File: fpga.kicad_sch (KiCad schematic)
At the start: 8 parts

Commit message: Added FPGA power component
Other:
- title: (none) -> Field-programmable gate array
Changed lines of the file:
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@@
 (kicad_sch (version 20230121) (generator eeschema)
   (paper "A3")
+  (title_block
+    (title "Field-programmable gate array")
+  )
   (wire (pts (xy 74.93 177.8) (xy 85.09 177.8))
     (stroke (width 0) (type default))

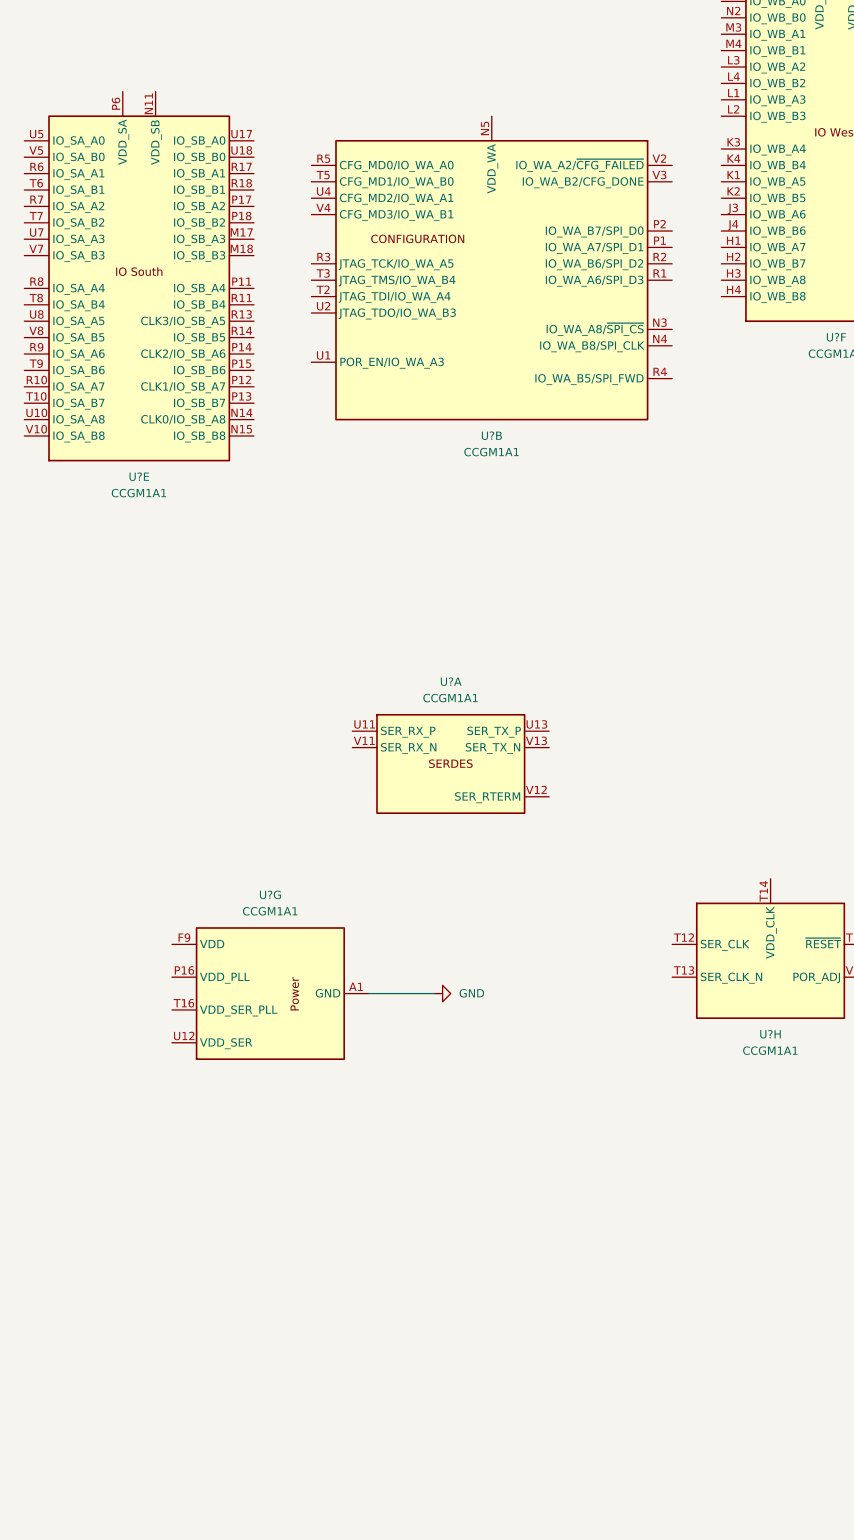
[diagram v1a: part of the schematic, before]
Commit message: Moved USB-C connector to root sheet
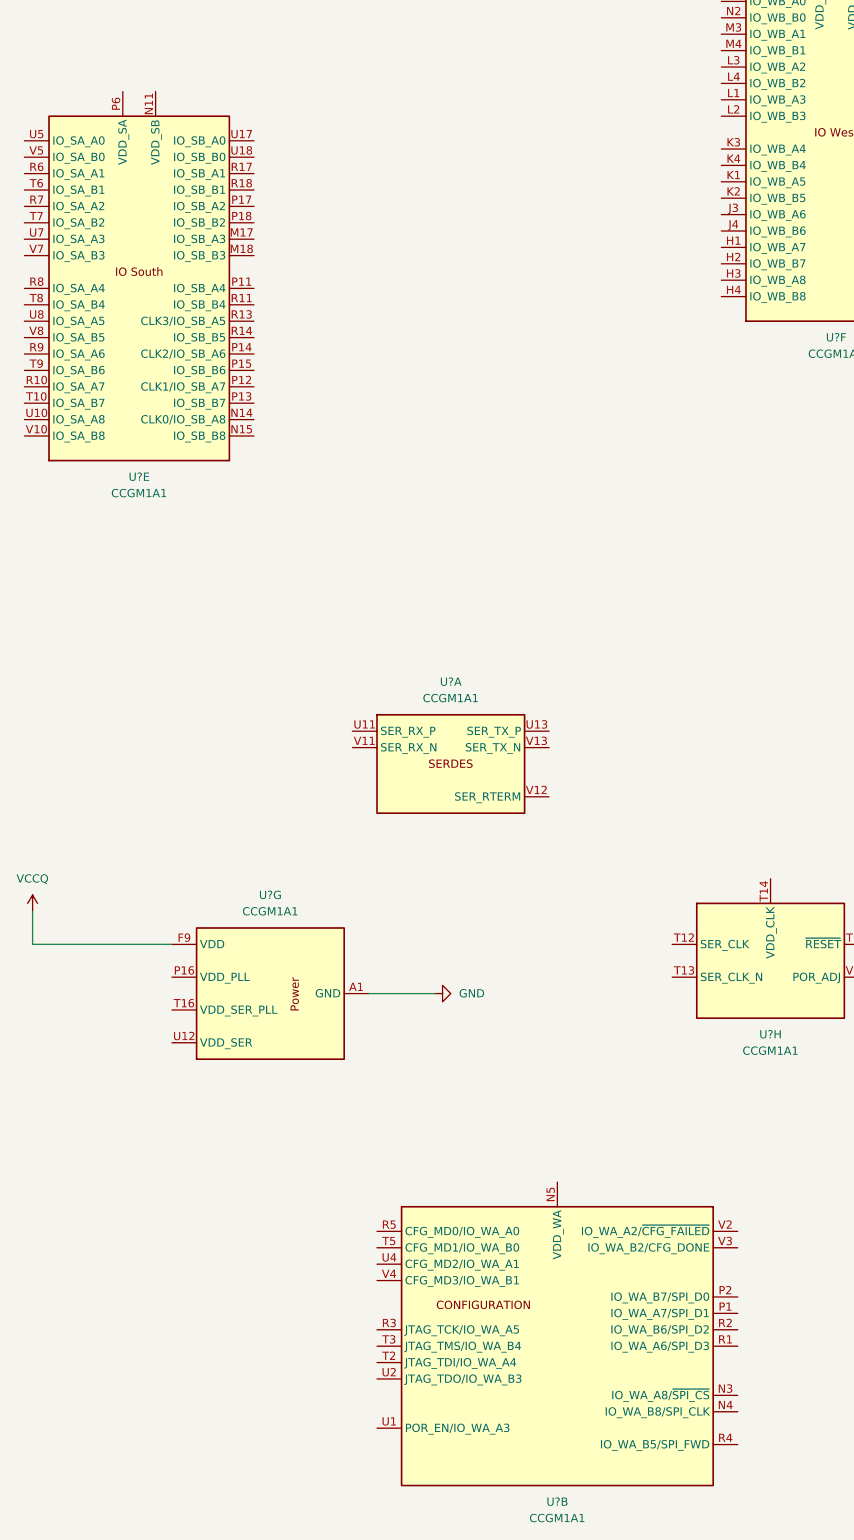
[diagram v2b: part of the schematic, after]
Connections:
- net VCCQ: now reaches U?.F9 (VDD), U?.G10 (VDD), U?.G12 (VDD), U?.G6 (VDD), U?.G8 (VDD), U?.H11 (VDD), U?.H13 (VDD), U?.H7 (VDD), U?.H9 (VDD), U?.J10 (VDD), U?.J12 (VDD), U?.J6 (VDD), U?.J8 (VDD), U?.K11 (VDD), U?.K13 (VDD), U?.K7 (VDD), U?.K9 (VDD), U?.L10 (VDD), U?.L12 (VDD), U?.L6 (VDD), U?.L8 (VDD), U?.M11 (VDD), U?.M13 (VDD), U?.M7 (VDD), U?.M9 (VDD), U?.N10 (VDD), U?.N6 (VDD), U?.N8 (VDD)
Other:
- moved on the sheet: U?B
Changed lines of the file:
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@@
+    (stroke (width 0) (type default))
+  )
+  (wire (pts (xy 22.86 170.18) (xy 44.45 170.18))
+    (stroke (width 0) (type default))
+  )
+  (wire (pts (xy 22.86 165.1) (xy 22.86 170.18))
     (stroke (width 0) (type default))
   )
@@
     )
   )
-  (symbol (lib_id "FPGA_CologneChip_GateMate:CCGM1A1") (at 93.98 67.31 0) (unit 2)
+  (symbol (lib_id "FPGA_CologneChip_GateMate:CCGM1A1") (at 104.14 232.41 0) (unit 2)
     (in_bom yes) (on_board yes) (dnp no) (fields_autoplaced)
-    (property "Reference" "U?" (at 93.98 91.44 0)
+    (property "Reference" "U?" (at 104.14 256.54 0)
       (effects (font (size 1.27 1.27)))
     )
-    (property "Value" "CCGM1A1" (at 93.98 93.98 0)
+    (property "Value" "CCGM1A1" (at 104.14 259.08 0)
       (effects (font (size 1.27 1.27)))
     )
-    (property "Footprint" "Package_BGA:BGA-324_15.0x15.0mm_Layout18x18_P0.8mm_Ball0.45mm_Pad0.4mm_NSMD" (at 88.9 50.8 0)
+    (property "Footprint" "Package_BGA:BGA-324_15.0x15.0mm_Layout18x18_P0.8mm_Ball0.45mm_Pad0.4mm_NSMD" (at 99.06 215.9 0)
       (effects (font (size 1.27 1.27)) hide)
     )
-    (property "Datasheet" "https://colognechip.com/docs/ds1001-gatemate1-datasheet-2022-05.pdf" (at 93.98 59.69 0)
+    (property "Datasheet" "https://colognechip.com/docs/ds1001-gatemate1-datasheet-2022-05.pdf" (at 104.14 224.79 0)
       (effects (font (size 1.27 1.27)) hide)
     )
@@
         )
       )
+    )
+  )
+  (symbol (lib_id "power:VCCQ") (at 22.86 165.1 0) (unit 1)
+    (in_bom yes) (on_board yes) (dnp no) (fields_autoplaced)
+    (property "Reference" "#PWR040" (at 22.86 168.91 0)
+      (effects (font (size 1.27 1.27)) hide)
+    )
+    (property "Value" "VCCQ" (at 22.86 160.02 0)
+      (effects (font (size 1.27 1.27)))
+    )
+    (property "Footprint" "" (at 22.86 165.1 0)
+      (effects (font (size 1.27 1.27)) hide)
+    )
+    (property "Datasheet" "" (at 22.86 165.1 0)
+      (effects (font (size 1.27 1.27)) hide)
+    )
+    (pin "1")
+    (instances
+      (project "drone"
+        (path "/d34d8324-c983-4098-8d7e-5c2fbd34794d/41f449fb-b4c2-4d53-966f-b49577e16db6"
+          (reference "#PWR040") (unit 1)
+        )
+      )

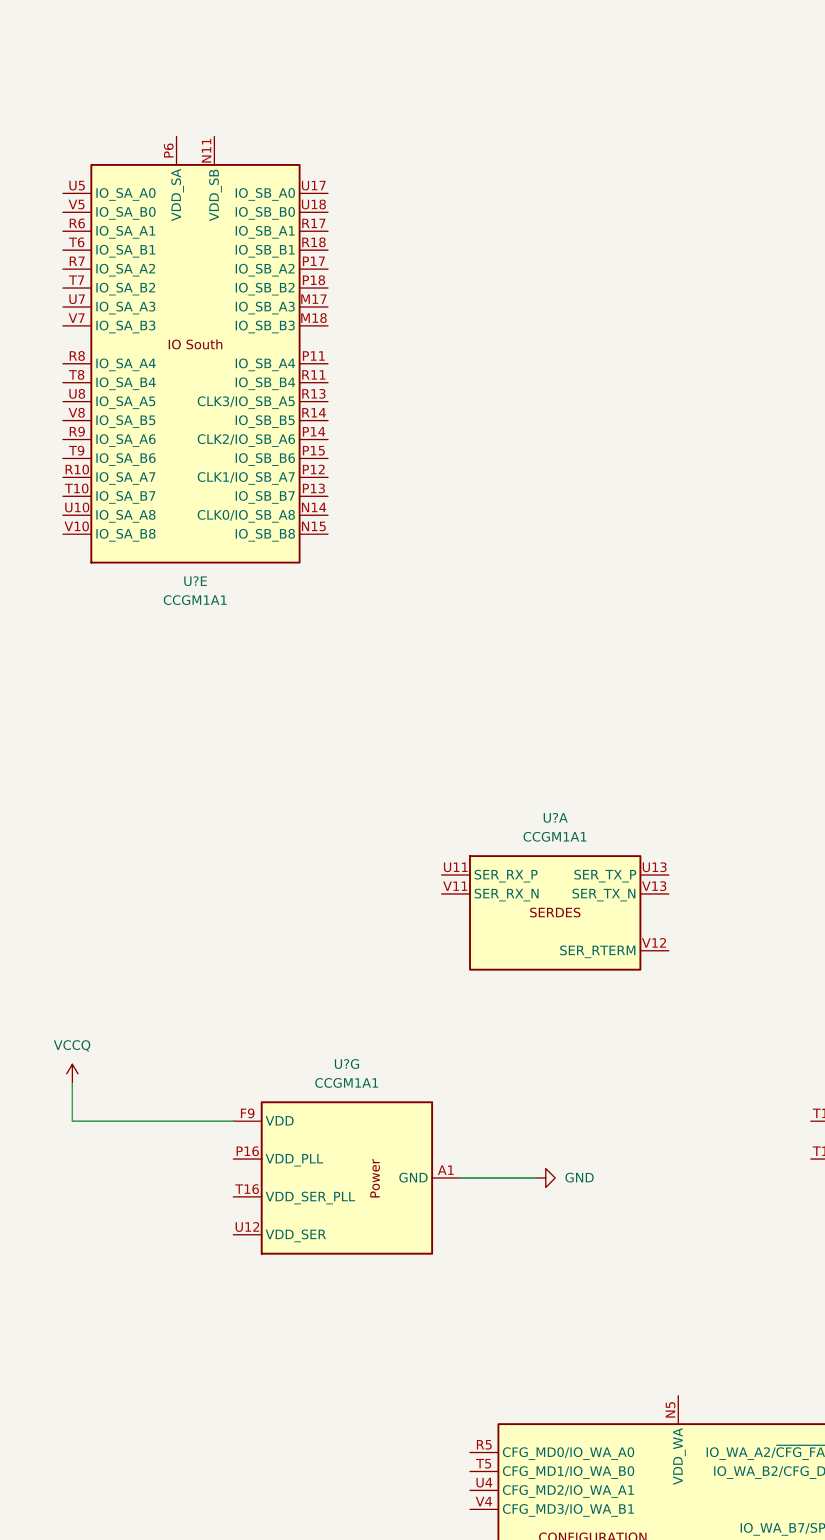
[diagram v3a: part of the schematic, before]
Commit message: Replacing global power labels with hierarchical pins
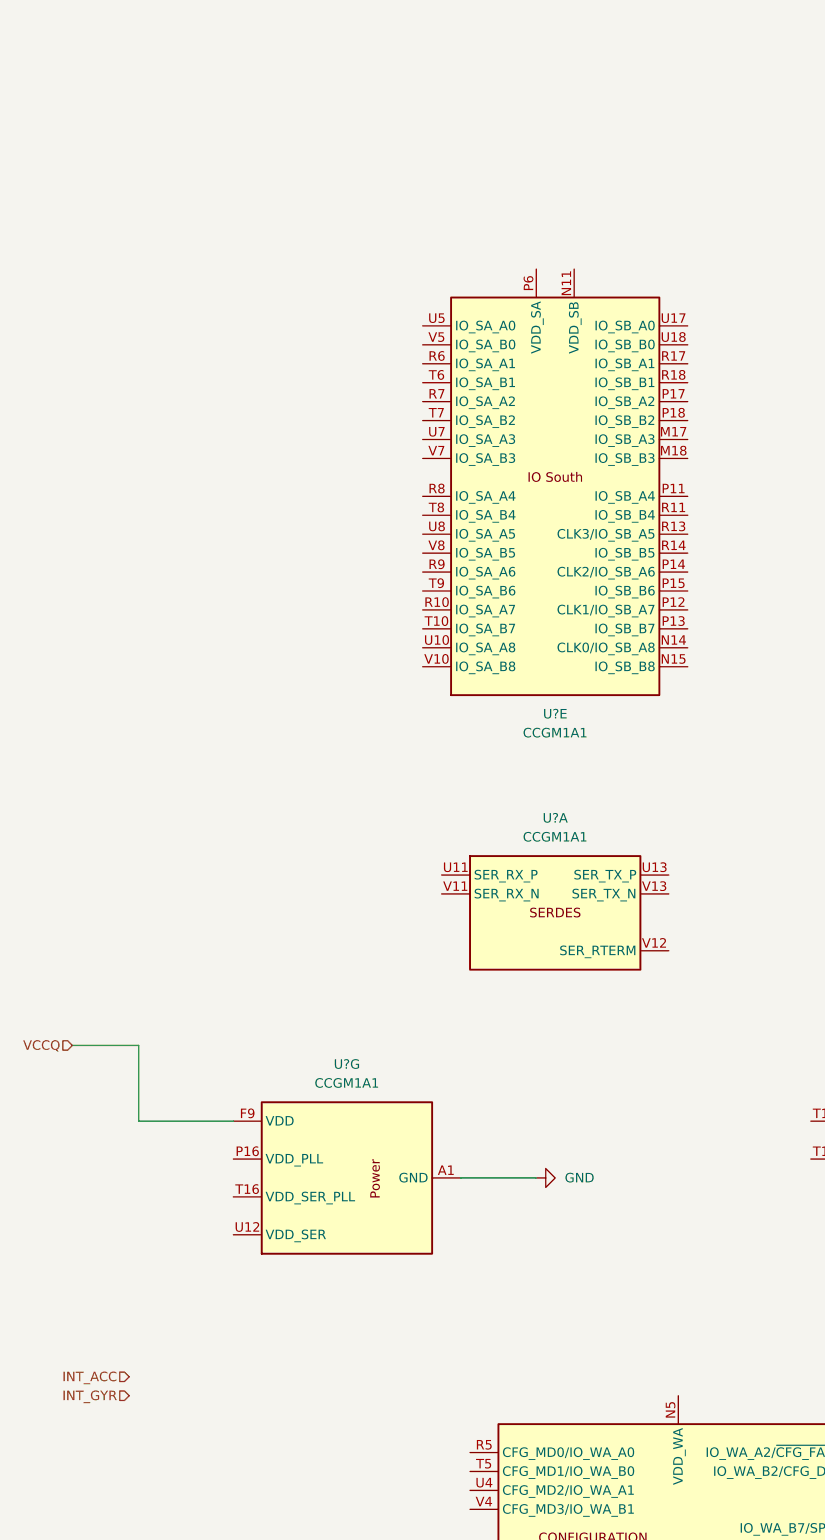
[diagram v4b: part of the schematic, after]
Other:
- moved on the sheet: U?E
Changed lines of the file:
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@@
     (stroke (width 0) (type default))
   )
-  (wire (pts (xy 22.86 170.18) (xy 44.45 170.18))
+  (wire (pts (xy 31.75 170.18) (xy 44.45 170.18))
     (stroke (width 0) (type default))
   )
-  (wire (pts (xy 22.86 165.1) (xy 22.86 170.18))
+  (wire (pts (xy 31.75 160.02) (xy 22.86 160.02))
     (stroke (width 0) (type default))
+  )
+  (wire (pts (xy 31.75 160.02) (xy 31.75 170.18))
+    (stroke (width 0) (type default))
+  )
+  (hierarchical_label "INT_ACC" (shape input) (at 30.48 204.47 180) (fields_autoplaced)
+    (effects (font (size 1.27 1.27)) (justify right))
+  )
+  (hierarchical_label "INT_GYR" (shape input) (at 30.48 207.01 180) (fields_autoplaced)
+    (effects (font (size 1.27 1.27)) (justify right))
+  )
+  (hierarchical_label "VCCQ" (shape input) (at 22.86 160.02 180) (fields_autoplaced)
+    (effects (font (size 1.27 1.27)) (justify right))
   )
   (symbol (lib_id "FPGA_CologneChip_GateMate:CCGM1A1") (at 87.63 142.24 0) (unit 1)
@@
     )
   )
-  (symbol (lib_id "power:VCCQ") (at 22.86 165.1 0) (unit 1)
+  (symbol (lib_id "FPGA_CologneChip_GateMate:CCGM1A1") (at 87.63 86.36 0) (unit 5)
     (in_bom yes) (on_board yes) (dnp no) (fields_autoplaced)
-    (property "Reference" "#PWR026" (at 22.86 168.91 0)
+    (property "Reference" "U?" (at 87.63 115.57 0)
+      (effects (font (size 1.27 1.27)))
+    )
+    (property "Value" "CCGM1A1" (at 87.63 118.11 0)
+      (effects (font (size 1.27 1.27)))
+    )
+    (property "Footprint" "Package_BGA:BGA-324_15.0x15.0mm_Layout18x18_P0.8mm_Ball0.45mm_Pad0.4mm_NSMD" (at 82.55 69.85 0)
       (effects (font (size 1.27 1.27)) hide)
     )
-    (property "Value" "VCCQ" (at 22.86 160.02 0)
-      (effects (font (size 1.27 1.27)))
-    )
-    (property "Footprint" "" (at 22.86 165.1 0)
+    (property "Datasheet" "https://colognechip.com/docs/ds1001-gatemate1-datasheet-2022-05.pdf" (at 87.63 78.74 0)
       (effects (font (size 1.27 1.27)) hide)
     )
-    (property "Datasheet" "" (at 22.86 165.1 0)
-      (effects (font (size 1.27 1.27)) hide)
-    )
-    (pin "1")
-    (instances
-      (project "drone"
-        (path "/d34d8324-c983-4098-8d7e-5c2fbd34794d/41f449fb-b4c2-4d53-966f-b49577e16db6"
-          (reference "#PWR026") (unit 1)
-        )
-      )
-    )
-  )
-  (symbol (lib_id "FPGA_CologneChip_GateMate:CCGM1A1") (at 39.37 68.58 0) (unit 5)
-    (in_bom yes) (on_board yes) (dnp no) (fields_autoplaced)
-    (property "Reference" "U?" (at 39.37 97.79 0)
-      (effects (font (size 1.27 1.27)))
-    )
-    (property "Value" "CCGM1A1" (at 39.37 100.33 0)
-      (effects (font (size 1.27 1.27)))
-    )
-    (property "Footprint" "Package_BGA:BGA-324_15.0x15.0mm_Layout18x18_P0.8mm_Ball0.45mm_Pad0.4mm_NSMD" (at 34.29 52.07 0)
-      (effects (font (size 1.27 1.27)) hide)
-    )
-    (property "Datasheet" "https://colognechip.com/docs/ds1001-gatemate1-datasheet-2022-05.pdf" (at 39.37 60.96 0)
-      (effects (font (size 1.27 1.27)) hide)
-    )

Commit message: Gathering memory components
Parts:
- added S1: PTS645SK43SMTR92LFS, PTS645SK43SMTR92LFS, symbol SamacSys_Parts:PTS645SK43SMTR92LFS
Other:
- note added: "3.2.2 FPGA reset using the POR module Using the POR module, in many cases no external components are required to ensure a safe reset of the GateMate FPGA. Figure 3.4 shows how to connect the reset pins in this case: • VDD_WA and VDD_CLK must be connected to 1.1 . . 2.7 V supply (might be different). • POR_EN has to be connected to VDD_WA or it can be left open due to the internal pullup resistor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"
- note added: "The POR must be enabled with POR_EN signal: 0: Reset state depends only on the RST_N signal. 1: FPGA changes from reset to operation state when RST_N is 1 and POR indicates VDD and VDD_CLK voltages are stable."
- note added: "The section you've provided describes the Power-On Reset (POR) feature of the GateMate™ FPGA. This is an important aspect of the FPGA's power-up sequence, ensuring that it starts up correctly under the right conditions. Here's a breakdown of what this means and how you would typically power on the FPGA: Reset Pin (RST_N): The FPGA has a reset pin labeled RST_N. This pin is active low, meaning it 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"
- moved on the sheet: U?B, U?H
